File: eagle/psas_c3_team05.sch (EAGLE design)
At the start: 88 parts, among them IC1 CP2102, U1 MIC5319 3.3V, U2 MCP73871, X1 32 MHz

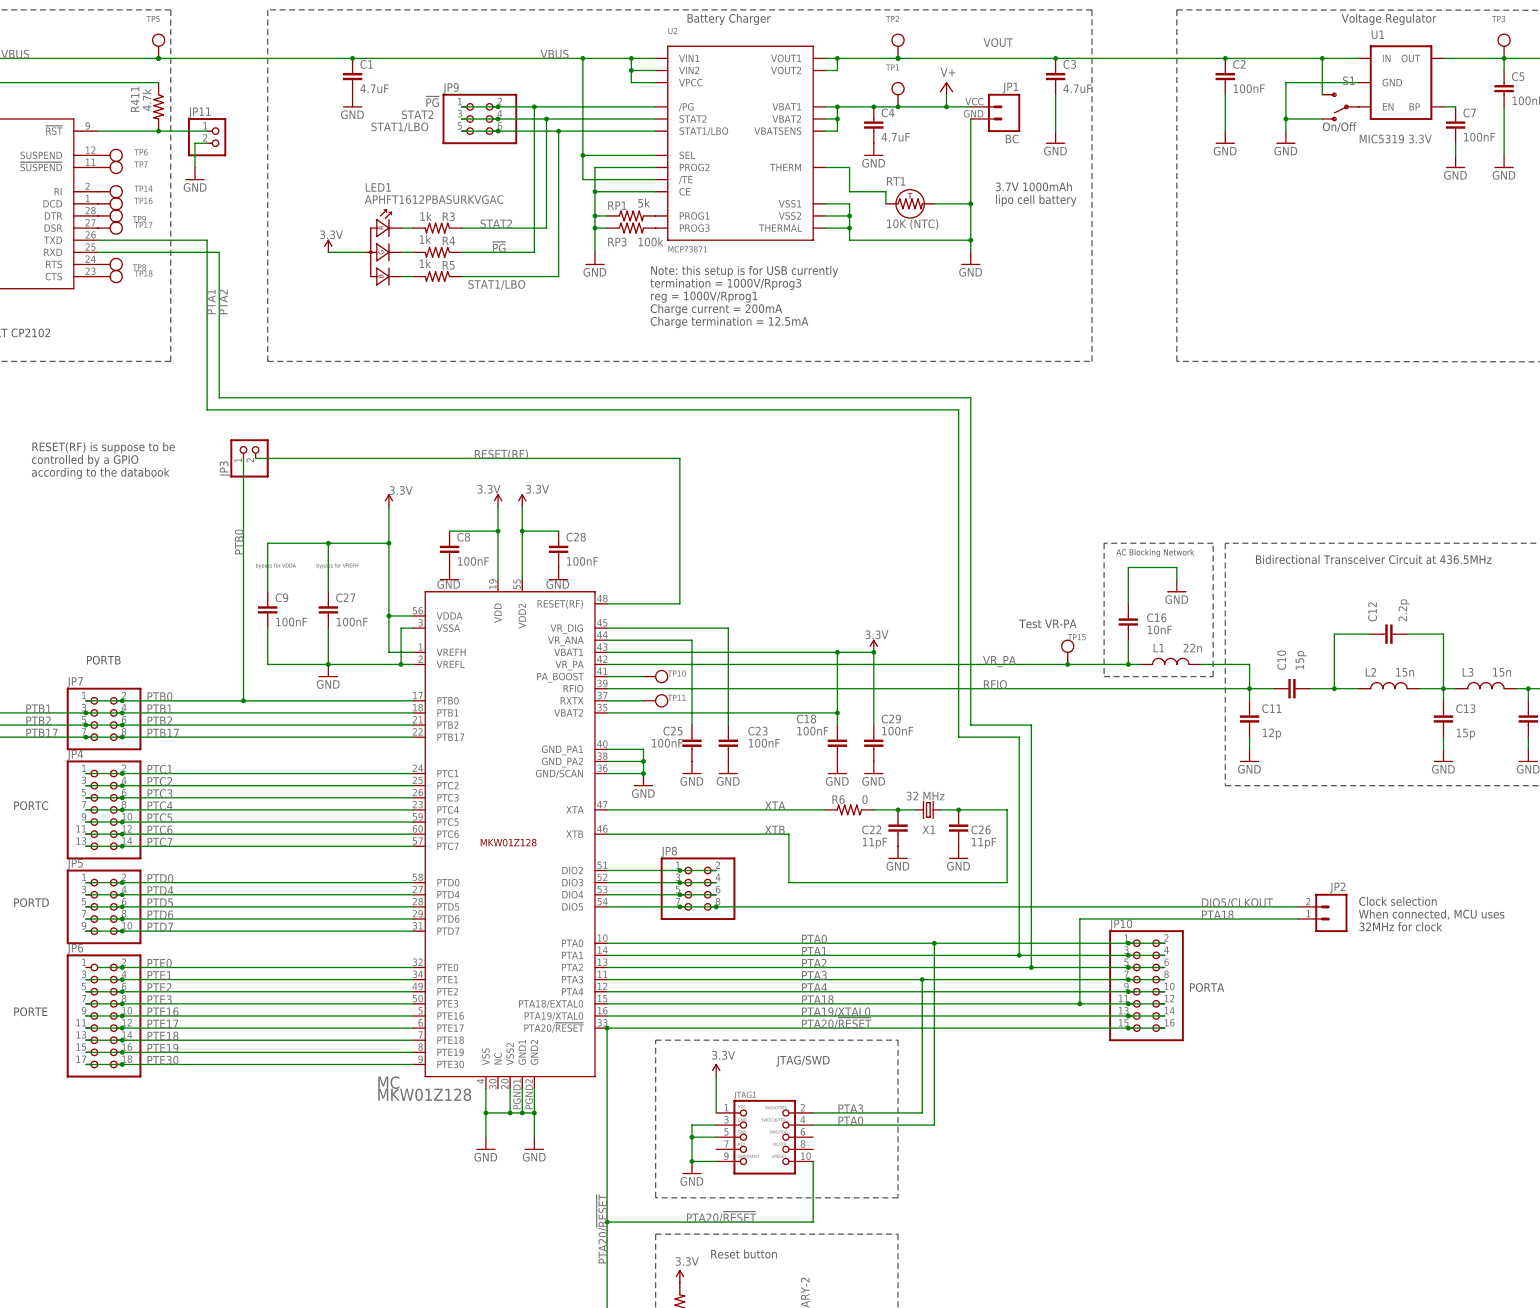
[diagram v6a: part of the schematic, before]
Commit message: Swtiched JTAG/SWD connector and added part values for missing values.
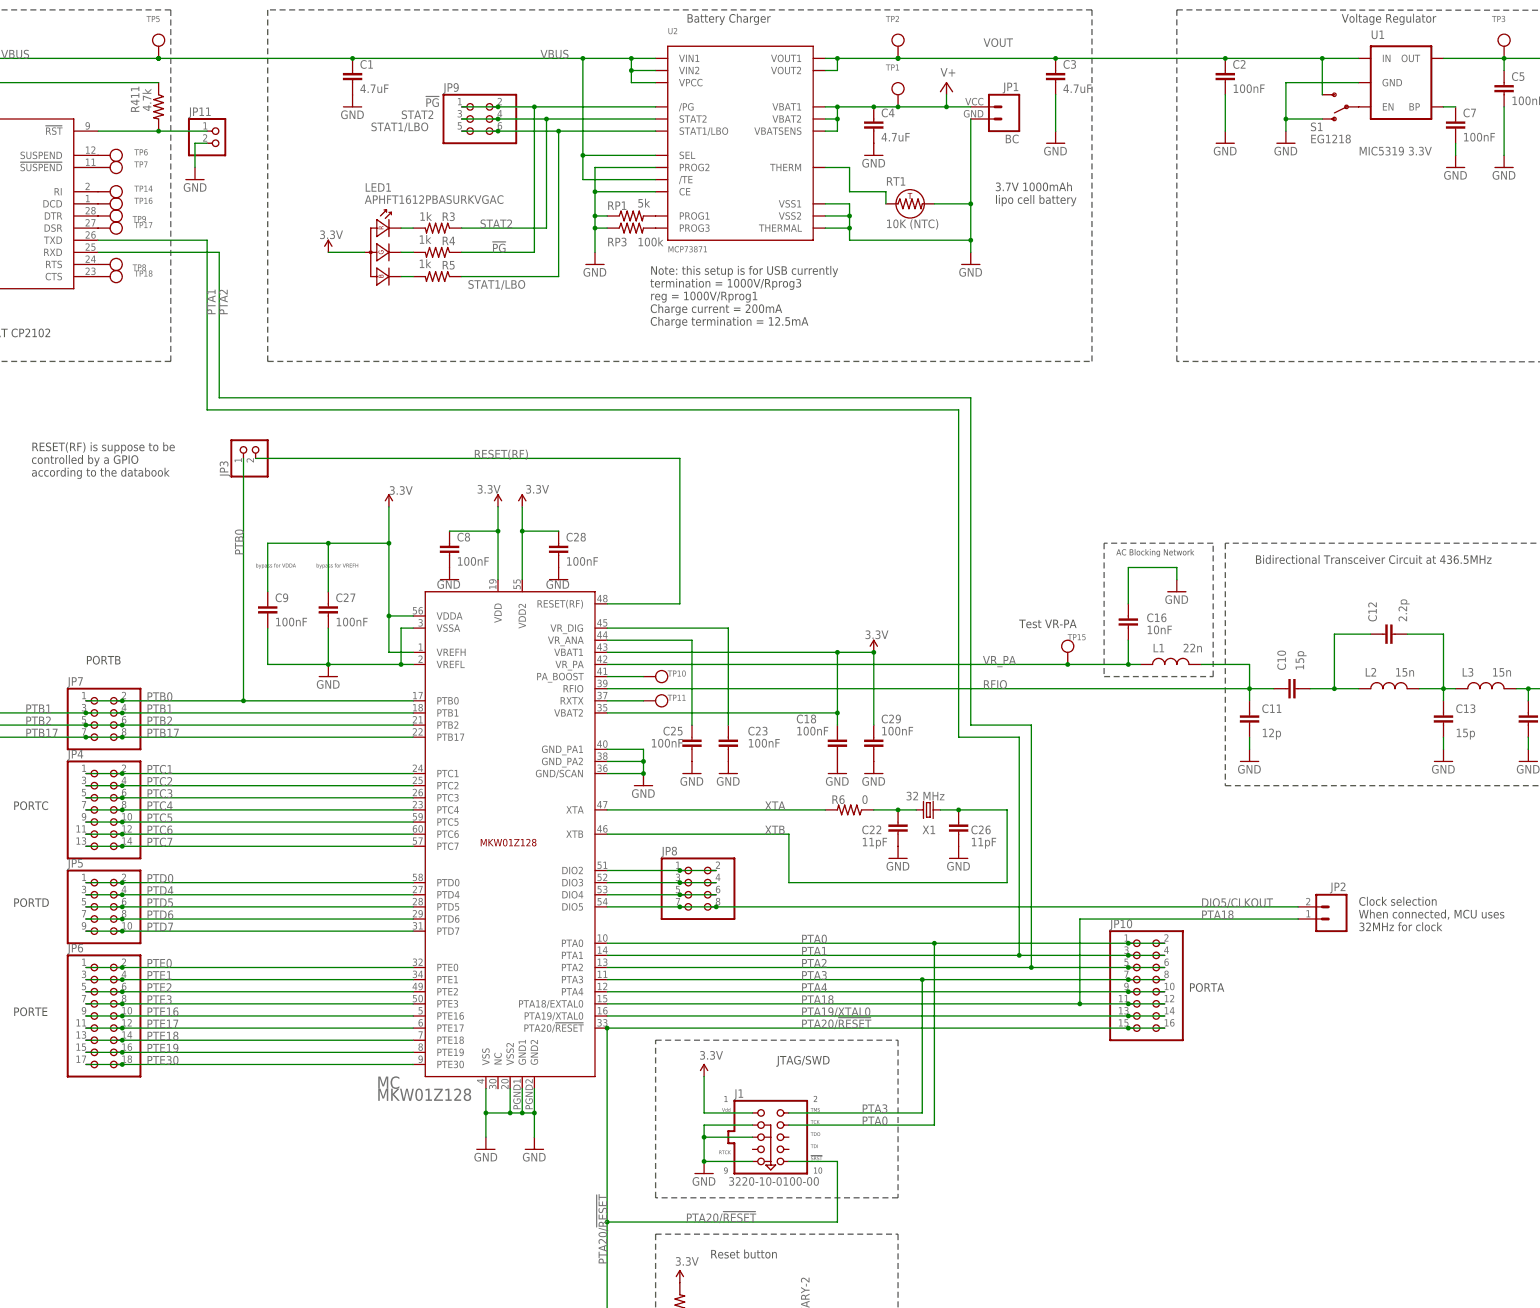
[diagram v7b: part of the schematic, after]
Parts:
- removed JTAG1: (no value), microbuilder:JTAG-CORTEXM3MOLEX
- added J1: 3220-10-0100-00, apdm-ic-v2:JTAG_ARM-10-50MIL
- S1: value (none) -> EG1218
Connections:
- net N$24 renamed CP2102_VDD
- net 3.3V: now also J1.VDD; no longer JTAG1.1
- net GND: now also J1.GND3, J1.GND5, J1.GND9; no longer JTAG1.3, JTAG1.5, JTAG1.9
- net PTA0: now also J1.TCK; no longer JTAG1.4
- net PTA20/!RESET: now also J1.SRST; no longer JTAG1.10
- net PTA3: now also J1.TMS; no longer JTAG1.2
- net PTE0: now also JP6.1
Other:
- note removed: "On/Off"
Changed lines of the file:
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@@
 <setting verticaltext="up"/>
 </settings>
-<grid distance="0.1" unitdist="inch" unit="inch" style="lines" multiple="1" display="no" altdistance="0.01" altunitdist="inch" altunit="inch"/>
+<grid distance="0.05" unitdist="inch" unit="inch" style="lines" multiple="2" display="yes" altdistance="0.01" altunitdist="inch" altunit="inch"/>
 <layers>
 <layer number="1" name="Top" color="4" fill="1" visible="no" active="no"/>
@@
 <part name="TP4" library="microbuilder" deviceset="TESTPOINT" device="ROUND0.5MM"/>
 <part name="GND10" library="Vibrogait_prototype" deviceset="GND" device=""/>
-<part name="S1" library="Vibrogait_prototype" deviceset="SWITCH-SPST" device="PTH"/>
+<part name="S1" library="Vibrogait_prototype" deviceset="SWITCH-SPST" device="PTH" value="EG1218"/>
 <part name="GND11" library="Vibrogait_prototype" deviceset="GND" device=""/>
 <part name="MC" library="psas_c3" deviceset="MKW01Z128" device="">
@@
 <part name="GND24" library="Vibrogait_prototype" deviceset="GND" device=""/>
 <part name="GND34" library="Vibrogait_prototype" deviceset="GND" device=""/>
-<part name="JTAG1" library="microbuilder" deviceset="JTAG-CORTEXM3" device="MOLEX"/>
 <part name="P+4" library="Vibrogait_prototype" deviceset="3.3V" device=""/>
 <part name="GND26" library="Vibrogait_prototype" deviceset="GND" device=""/>
@@
 <part name="R9" library="rcl_custom" deviceset="R-US_" device="0603-B-NOSILK" value="1k"/>
 <part name="P+9" library="Vibrogait_prototype" deviceset="3.3V" device=""/>
+<part name="J1" library="apdm-ic-v2" deviceset="JTAG_ARM-10-*" device="50MIL" value="3220-10-0100-00">
+<attribute name="DIGIKEY-PN" value="1175-1627-ND"/>
+<attribute name="MFG" value="CNC Tech"/>
+<attribute name="MFG-PN" value="3220-10-0100-00"/>
+</part>
 </parts>
 <sheets>
@@
 Charge current = 200mA
 Charge termination = 12.5mA</text>
-<text x="411.48" y="335.28" size="1.778" layer="97">On/Off</text>
 <wire x1="381" y1="360.68" x2="508.254" y2="360.553" width="0.1524" layer="97" style="dashdot"/>
 <wire x1="508.254" y1="360.553" x2="508.254" y2="286.893" width="0.1524" layer="97" style="dashdot"/>
@@
 <instance part="U1" gate="G$1" x="429.26" y="345.44" smashed="yes">
 <attribute name="NAME" x="421.64" y="354.584" size="1.778" layer="95"/>
-<attribute name="VALUE" x="419.1" y="332.74" size="1.778" layer="96"/>
+<attribute name="VALUE" x="419.1" y="330.2" size="1.778" layer="96"/>
 </instance>
 <instance part="JP1" gate="G$1" x="345.44" y="337.82" smashed="yes" rot="MR0">
@@
 </instance>
 <instance part="S1" gate="1" x="416.56" y="340.36" smashed="yes" rot="R180">
-<attribute name="NAME" x="418.465" y="346.71" size="1.778" layer="95" rot="R180"/>
-<attribute name="VALUE" x="419.1" y="336.55" size="1.778" layer="96" rot="R180"/>
+<attribute name="NAME" x="408.94" y="335.28" size="1.778" layer="95"/>
+<attribute name="VALUE" x="408.94" y="332.74" size="1.778" layer="96"/>
 </instance>
 <instance part="GND11" gate="1" x="317.5" y="330.2" smashed="yes">
@@
 <attribute name="VALUE" x="284.48" y="198.12" size="1.778" layer="96"/>
 </instance>
-<instance part="JTAG1" gate="G$1" x="294.64" y="119.38" smashed="yes">
-<attribute name="NAME" x="288.29" y="132.715" size="1.27" layer="95"/>
-<attribute name="VALUE" x="288.29" y="114.935" size="1.27" layer="96"/>
-</instance>
-<instance part="P+4" gate="G$1" x="284.48" y="137.16" smashed="yes">
-<attribute name="VALUE" x="283.464" y="140.716" size="1.778" layer="96"/>
-</instance>
-<instance part="GND26" gate="1" x="279.4" y="116.84" smashed="yes">
-<attribute name="VALUE" x="276.86" y="114.3" size="1.778" layer="96"/>
+<instance part="P+4" gate="G$1" x="281.94" y="137.16" smashed="yes">
+<attribute name="VALUE" x="280.924" y="140.716" size="1.778" layer="96"/>
+</instance>
+<instance part="GND26" gate="1" x="281.94" y="116.84" smashed="yes">
+<attribute name="VALUE" x="279.4" y="114.3" size="1.778" layer="96"/>
 </instance>
 <instance part="FRAME1" gate="G$1" x="0" y="0"/>
@@
 <instance part="P+9" gate="G$1" x="119.38" y="236.22" smashed="yes">
 <attribute name="VALUE" x="119.38" y="238.76" size="1.778" layer="96"/>
+</instance>
+<instance part="J1" gate="J" x="295.91" y="124.46" smashed="yes">
+<attribute name="DIGIKEY-PN" x="295.91" y="124.46" size="1.778" layer="96" display="off"/>
+<attribute name="MFG" x="295.91" y="124.46" size="1.778" layer="96" display="off"/>
+<attribute name="MFG-PN" x="295.91" y="124.46" size="1.778" layer="96" display="off"/>
+<attribute name="NAME" x="288.29" y="132.715" size="1.778" layer="95"/>
+<attribute name="VALUE" x="287.02" y="114.3" size="1.778" layer="96"/>
 </instance>
 </instances>
@@
 </segment>
 <segment>
-<pinref part="JTAG1" gate="G$1" pin="9"/>
 <pinref part="GND26" gate="1" pin="GND"/>
-<wire x1="279.4" y1="119.38" x2="284.48" y2="119.38" width="0.1524" layer="91"/>
-<pinref part="JTAG1" gate="G$1" pin="3"/>
-<wire x1="284.48" y1="127" x2="279.4" y2="127" width="0.1524" layer="91"/>
-<wire x1="279.4" y1="127" x2="279.4" y2="124.46" width="0.1524" layer="91"/>
-<junction x="279.4" y="119.38"/>
-<pinref part="JTAG1" gate="G$1" pin="5"/>
-<wire x1="279.4" y1="124.46" x2="279.4" y2="119.38" width="0.1524" layer="91"/>
-<wire x1="284.48" y1="124.46" x2="279.4" y2="124.46" width="0.1524" layer="91"/>
-<junction x="279.4" y="124.46"/>
+<wire x1="281.94" y1="127" x2="281.94" y2="124.46" width="0.1524" layer="91"/>
+<junction x="281.94" y="119.38"/>
+<wire x1="281.94" y1="124.46" x2="281.94" y2="119.38" width="0.1524" layer="91"/>
+<junction x="281.94" y="124.46"/>
+<pinref part="J1" gate="J" pin="GND9"/>
+<wire x1="281.94" y1="119.38" x2="292.1" y2="119.38" width="0.1524" layer="91"/>
+<pinref part="J1" gate="J" pin="GND5"/>
+<wire x1="292.1" y1="124.46" x2="281.94" y2="124.46" width="0.1524" layer="91"/>
+<pinref part="J1" gate="J" pin="GND3"/>
+<wire x1="281.94" y1="127" x2="292.1" y2="127" width="0.1524" layer="91"/>
 </segment>
 <segment>
@@
 </segment>
 <segment>
-<pinref part="JTAG1" gate="G$1" pin="1"/>
 <pinref part="P+4" gate="G$1" pin="3.3V"/>
-<wire x1="284.48" y1="137.16" x2="284.48" y2="129.54" width="0.1524" layer="91"/>
+<wire x1="281.94" y1="137.16" x2="281.94" y2="129.54" width="0.1524" layer="91"/>
+<pinref part="J1" gate="J" pin="VDD"/>
+<wire x1="292.1" y1="129.54" x2="281.94" y2="129.54" width="0.1524" layer="91"/>
 </segment>
 <segment>
@@
 <wire x1="261.62" y1="157.48" x2="327.66" y2="157.48" width="0.1524" layer="91"/>
 <wire x1="327.66" y1="157.48" x2="327.66" y2="129.54" width="0.1524" layer="91"/>
-<pinref part="JTAG1" gate="G$1" pin="2"/>
-<wire x1="304.8" y1="129.54" x2="327.66" y2="129.54" width="0.1524" layer="91"/>
+<wire x1="299.72" y1="129.54" x2="327.66" y2="129.54" width="0.1524" layer="91"/>
 <label x="302.26" y="157.48" size="1.778" layer="95"/>
 <pinref part="JP10" gate="A" pin="7"/>
@@
 <wire x1="378.46" y1="157.48" x2="370.84" y2="157.48" width="0.1524" layer="91"/>
 <junction x="370.84" y="157.48"/>
-<label x="309.88" y="129.54" size="1.778" layer="95"/>
+<label x="314.96" y="129.54" size="1.778" layer="95"/>
+<pinref part="J1" gate="J" pin="TMS"/>
 </segment>
 </net>
@@
 <wire x1="261.62" y1="165.1" x2="330.2" y2="165.1" width="0.1524" layer="91"/>
 <wire x1="330.2" y1="165.1" x2="330.2" y2="127" width="0.1524" layer="91"/>
-<pinref part="JTAG1" gate="G$1" pin="4"/>
-<wire x1="304.8" y1="127" x2="330.2" y2="127" width="0.1524" layer="91"/>
+<wire x1="299.72" y1="127" x2="330.2" y2="127" width="0.1524" layer="91"/>
 <label x="302.26" y="165.1" size="1.778" layer="95"/>
-<label x="309.88" y="127" size="1.778" layer="95"/>
+<label x="314.96" y="127" size="1.778" layer="95"/>
 <pinref part="JP10" gate="A" pin="1"/>
 <wire x1="330.2" y1="165.1" x2="370.84" y2="165.1" width="0.1524" layer="91"/>
@@
 <wire x1="378.46" y1="165.1" x2="370.84" y2="165.1" width="0.1524" layer="91"/>
 <junction x="370.84" y="165.1"/>
+<pinref part="J1" gate="J" pin="TCK"/>
 </segment>
 </net>
@@
 <pinref part="MC" gate="G$1" pin="PTA20/!RESET"/>
 <wire x1="261.62" y1="147.32" x2="261.62" y2="106.68" width="0.1524" layer="91"/>
-<pinref part="JTAG1" gate="G$1" pin="10"/>
-<wire x1="304.8" y1="119.38" x2="304.8" y2="106.68" width="0.1524" layer="91"/>
-<wire x1="304.8" y1="106.68" x2="261.62" y2="106.68" width="0.1524" layer="91"/>
+<wire x1="309.88" y1="119.38" x2="309.88" y2="106.68" width="0.1524" layer="91"/>
+<wire x1="309.88" y1="106.68" x2="261.62" y2="106.68" width="0.1524" layer="91"/>
 <label x="302.26" y="147.32" size="1.778" layer="95"/>
 <wire x1="261.62" y1="106.68" x2="261.62" y2="81.28" width="0.1524" layer="91"/>
@@
 <wire x1="378.46" y1="147.32" x2="370.84" y2="147.32" width="0.1524" layer="91"/>
 <junction x="370.84" y="147.32"/>
+<pinref part="J1" gate="J" pin="SRST"/>
+<wire x1="299.72" y1="119.38" x2="309.88" y2="119.38" width="0.1524" layer="91"/>
 </segment>
 </net>
@@
 </segment>
 </net>
-<net name="N$24" class="0">
+<net name="CP2102_VDD" class="0">
 <segment>
 <pinref part="C24" gate="CE" pin="1"/>
@@
 <wire x1="160.02" y1="160.02" x2="220.98" y2="160.02" width="0.1524" layer="91"/>
 <label x="165.1" y="160.02" size="1.778" layer="95"/>
-<wire x1="154.94" y1="160.02" x2="160.02" y2="160.02" width="0.1524" layer="91"/>
+<wire x1="152.4" y1="160.02" x2="160.02" y2="160.02" width="0.1524" layer="91"/>
 <junction x="160.02" y="160.02"/>
-</segment>
-</net>
+<pinref part="JP6" gate="A" pin="1"/>
+</segment>
+</net>

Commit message: major board cleanup and shrinkage. OOPS: just found out the uC pinout is wrong. Committing before doing that change.
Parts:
- C24: device rcl_custom:C-EU0603-B-NOSILK -> rcl_custom:C-EU0805-B-NOSILK
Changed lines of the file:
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@@
 <part name="R5" library="rcl_custom" deviceset="R-US_" device="0603-B-NOSILK" value="1k"/>
 <part name="TP5" library="microbuilder" deviceset="TESTPOINT" device="ROUND0.5MM"/>
-<part name="C24" library="rcl_custom" deviceset="C-EU" device="0603-B-NOSILK" value="4.7uF"/>
+<part name="C24" library="rcl_custom" deviceset="C-EU" device="0805-B-NOSILK" value="4.7uF"/>
 <part name="GND16" library="Vibrogait_prototype" deviceset="GND" device=""/>
 <part name="GND23" library="Vibrogait_prototype" deviceset="GND" device=""/>
